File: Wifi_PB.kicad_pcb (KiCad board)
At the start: 2 copper layers, 100 x 49.7 mm, 163 parts, among them P1 CONN_01X02, P10 CONN_01X01, P12 CONN_01X04, P13 CONN_01X04, P14 CONN_01X04, P15 USB_MINI, P16 CONN_01X01, P17 CONN_01X01, P18 CONN_01X01, P19 CONN_01X01, P2 CONN_01X03, P3 CONN_01X03, P4 CONN_01X03, P5 CONN_01X03, P6 CONN_01X01, P7 CONN_01X01, P8 CONN_01X01, P9 CONN_01X01, Q1 SMBT3904, Q10 BC849, Q11 NX2301P, Q2 SMBT3904, Q3 BSS138, Q4 BSS138, Q5 SMBT3904, Q6 SMBT3904, Q7 SMBT3904, Q8 SMBT3904, Q9 SMBT3904, SW1 Pulsador_2p, SW2 Pulsador_2p, SW3 Pulsador_2p, SW4 Pulsador_2p, U1 MCP73831T, U10 Matriz_5x7_Anodo_Filas, U11 40106, U12 MCP1640, U2 LD1117S33TR, U3 CH340G, U4 ESP8266, U5 MMA7660FC, U6 MCP23017, U7 MCP23017, U8 MCP3204, U9 PCA9551, Y1 Cristal

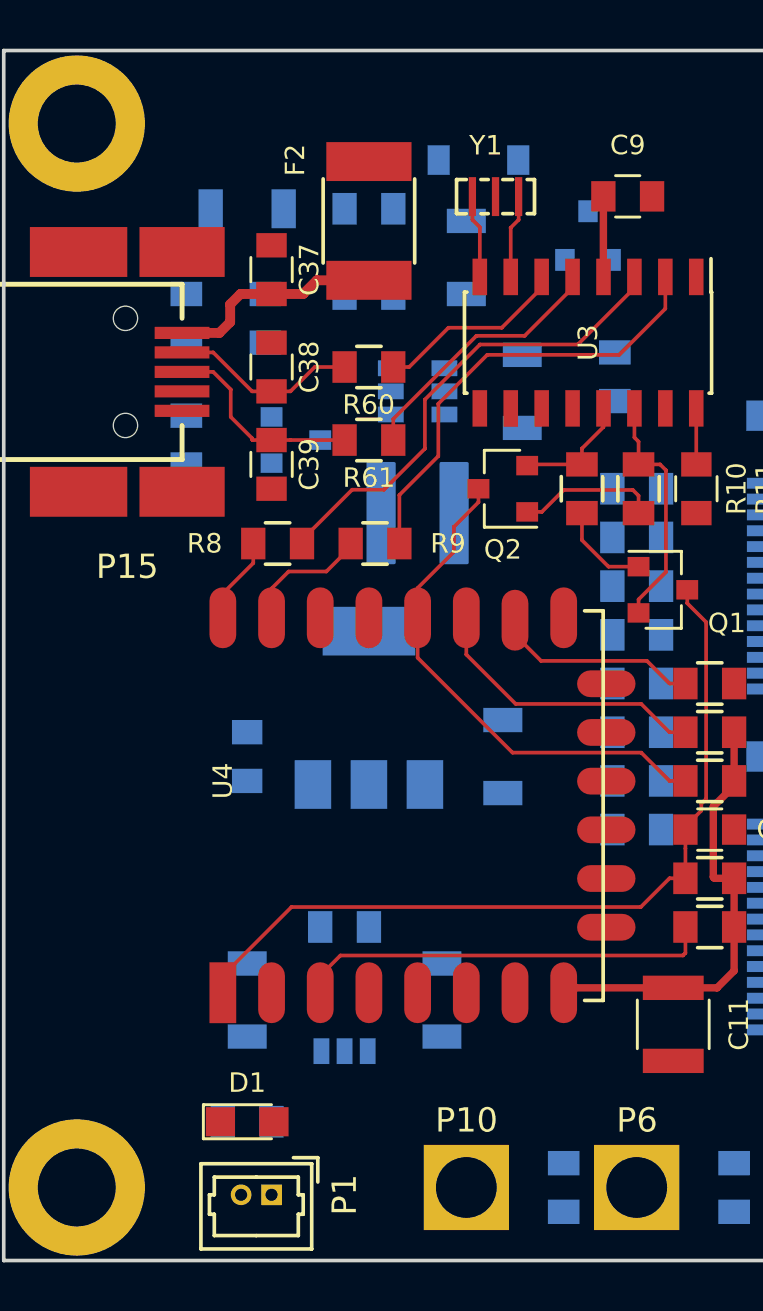
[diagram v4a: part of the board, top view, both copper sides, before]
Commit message: realizado el trazado de los reguladores
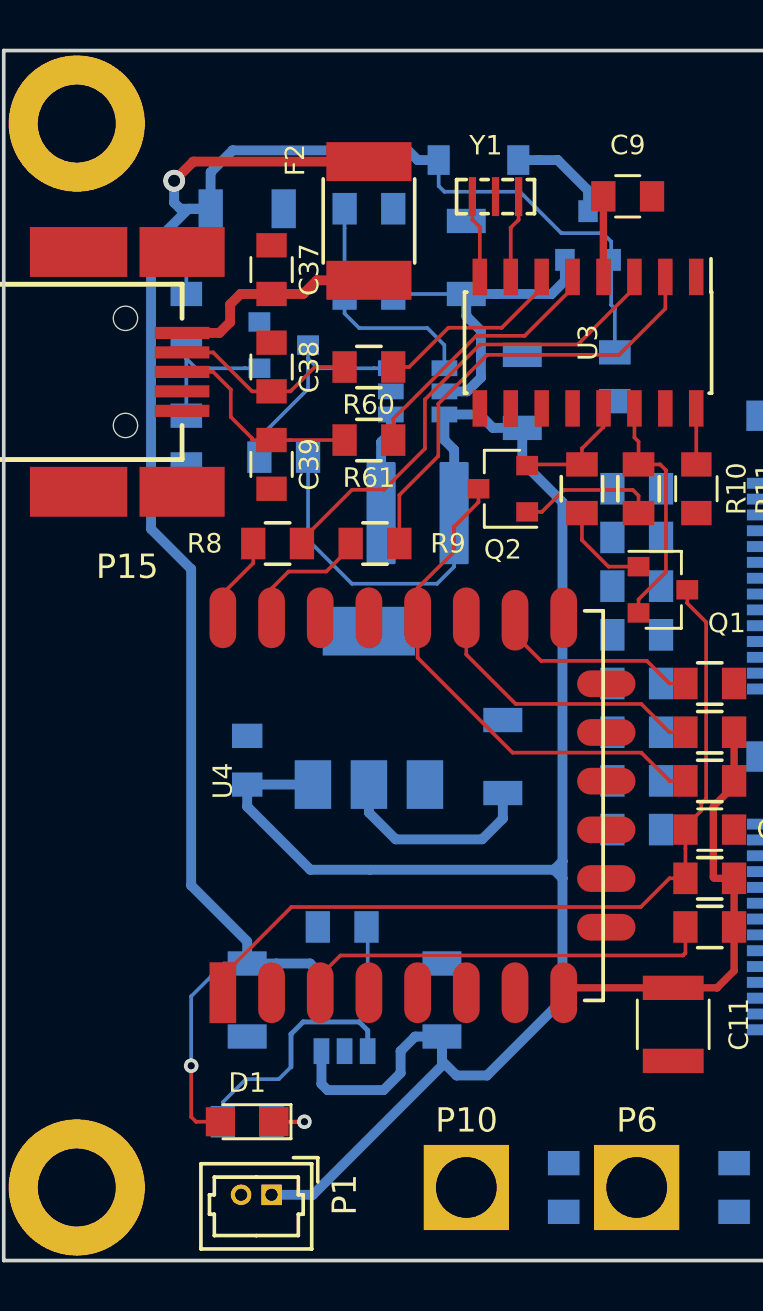
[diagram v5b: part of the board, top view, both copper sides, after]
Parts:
- moved R56 5.75 mm to (65.5, 51.7), turned to 0 degrees
- moved Q10 3.93 mm to (65.5, 47.1)
- moved C2 0.15 mm to (64.0, 64.2)
- moved R2 0.10 mm to (67.9, 71.0)
- turned D1 to 180 degrees
- turned R1 to 0 degrees
- turned R55 to 270 degrees
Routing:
- net VBATT: track 0.00 -> 88.5 mm
- net VUSB: track 0.00 -> 87.3 mm, vias 0 -> 2
- net V5VBOOST: track 0.00 -> 13.5 mm
- net Net-(R1-Pad1): track 0.00 -> 9.90 mm
- net Net-(R57-Pad2): track 0.00 -> 9.89 mm
- net Net-(Q10-Pad3): track 0.00 -> 8.99 mm
- net +3V3: track 21.8 -> 30.3 mm
- net Net-(Q10-Pad1): track 0.00 -> 6.16 mm
- net +5V: track 2.30 -> 6.54 mm
- net Net-(L2-Pad2): track 0.00 -> 4.22 mm
- net Net-(R2-Pad1): track 0.00 -> 2.99 mm
- net Net-(D1-Pad1): track 0.00 -> 2.60 mm, vias 0 -> 1

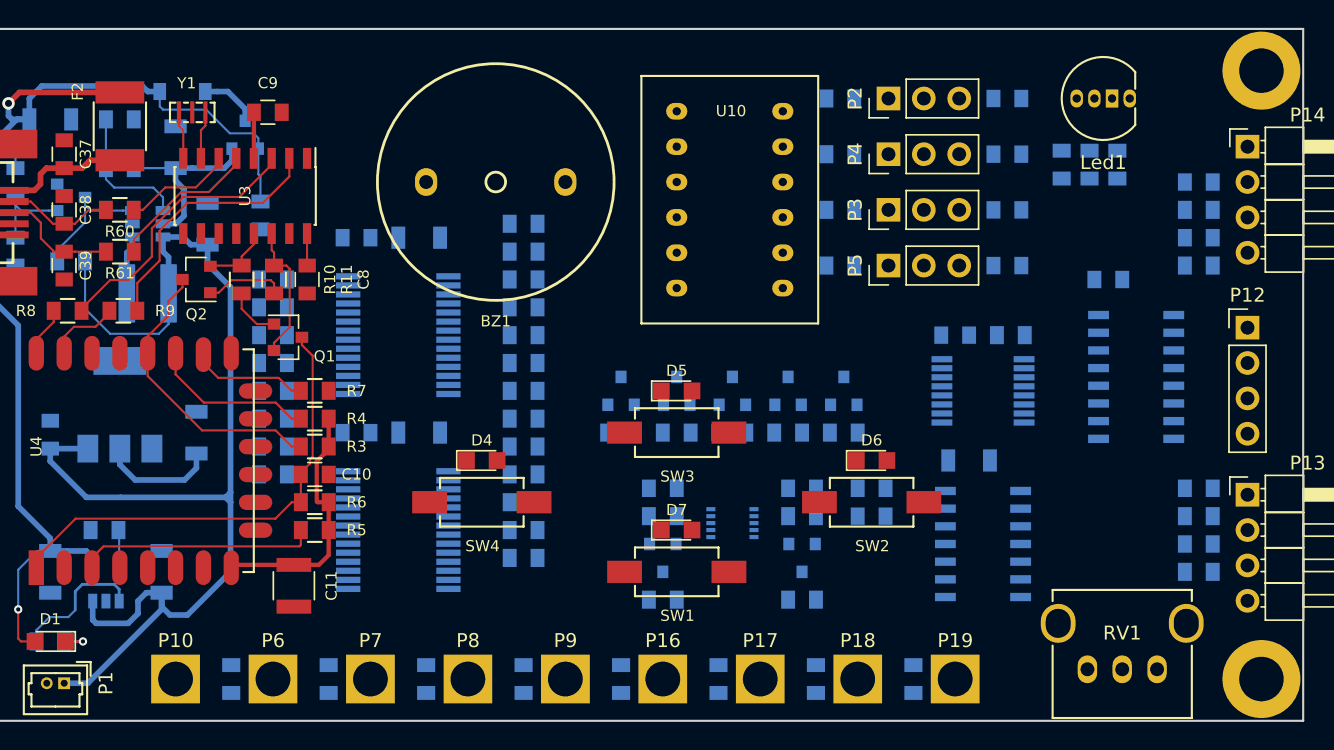
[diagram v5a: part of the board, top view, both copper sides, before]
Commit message: modificado conexion led rgb para mejorar trazado
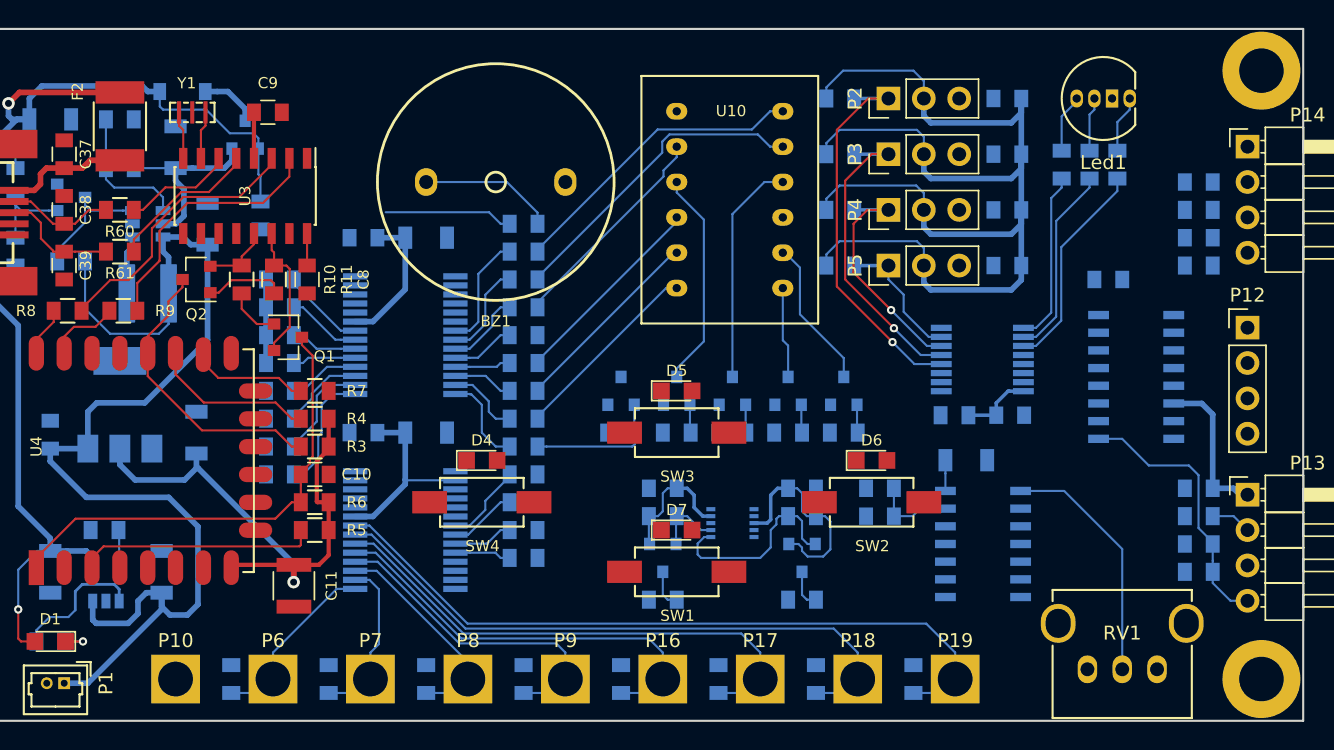
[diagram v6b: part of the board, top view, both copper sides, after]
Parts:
- moved R16 7.03 mm to (129.0, 62.7)
- moved C21 6.98 mm to (133.0, 62.7)
- moved R22 6.02 mm to (80.5, 67.0)
- moved R25 6.02 mm to (80.5, 61.0)
- moved P3 4.00 mm to (124.2, 44.0)
- moved P4 4.00 mm to (124.2, 48.0)
- moved U9 2.25 mm to (131.0, 58.7), turned to 0 degrees
- moved R23 2.06 mm to (80.5, 65.0)
- moved R24 2.06 mm to (80.5, 63.0)
- moved C18 0.60 mm to (123.6, 70.0)
- moved C19 0.60 mm to (123.6, 68.0)
- moved C14 0.50 mm to (91.0, 50.0)
- moved C15 0.50 mm to (91.0, 64.0)
- moved C16 0.50 mm to (86.5, 50.0)
- moved C17 0.50 mm to (86.5, 64.0)
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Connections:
- U9 pad 11: LED_GREEN -> LED_RED
- U9 pad 9: LED_RED -> LED_GREEN
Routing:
- net +5V: track 6.54 -> 152.2 mm
- net PD7: track 0.00 -> 52.2 mm
- net +3V3: track 30.3 -> 75.3 mm, vias 0 -> 1
- net PD6: track 0.00 -> 44.9 mm
- net PD5: track 0.00 -> 37.7 mm
- net PD4: track 0.00 -> 30.4 mm
- net SERVO1: track 0.00 -> 28.2 mm, vias 0 -> 1
- net PD3: track 0.00 -> 23.1 mm
- net Net-(R26-Pad1): track 0.00 -> 22.9 mm
- net SERVO2: track 0.00 -> 22.6 mm, vias 0 -> 1
- net Net-(R31-Pad1): track 0.00 -> 21.9 mm
- net Net-(C31-Pad1): track 0.00 -> 19.5 mm
- net CH0: track 0.00 -> 17.7 mm
- net SERVO3: track 0.00 -> 17.4 mm, vias 0 -> 1
- net Net-(Q7-Pad3): track 0.00 -> 16.3 mm
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
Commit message: añadida LDR. Finalizado trazado provisional
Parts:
- added Gnd-Via: VAL**, Vias:Gnd-Via, F.Cu at (64.1, 69.0)
- added Gnd-Via: VAL**, Vias:Gnd-Via, F.Cu at (110.4, 74.6)
- added Gnd-Via: VAL**, Vias:Gnd-Via, F.Cu at (110.3, 77.6)
- added Gnd-Via: VAL**, Vias:Gnd-Via, F.Cu at (102.3, 75.9)
- added Gnd-Via: VAL**, Vias:Gnd-Via, F.Cu at (100.1, 74.8)
- added Gnd-Via: VAL**, Vias:Gnd-Via, F.Cu at (112.2, 69.5)
- added Gnd-Via: VAL**, Vias:Gnd-Via, F.Cu at (113.6, 71.1)
- added Gnd-Via: VAL**, Vias:Gnd-Via, F.Cu at (121.1, 67.6)
- added Gnd-Via: VAL**, Vias:Gnd-Via, F.Cu at (74.1, 56.4)
- added Gnd-Via: VAL**, Vias:Gnd-Via, F.Cu at (76.3, 62.7)
- added Gnd-Via: VAL**, Vias:Gnd-Via, F.Cu at (77.6, 56.2)
- added Gnd-Via: VAL**, Vias:Gnd-Via, F.Cu at (67.8, 67.5)
- added Gnd-Via: VAL**, Vias:Gnd-Via, F.Cu at (76.4, 55.8)
- added Gnd-Via: VAL**, Vias:Gnd-Via, F.Cu at (86.8, 48.0)
- added Gnd-Via: VAL**, Vias:Gnd-Via, F.Cu at (78.4, 57.9)
- added Gnd-Via: VAL**, Vias:Gnd-Via, F.Cu at (76.7, 76.5)
- added Gnd-Via: VAL**, Vias:Gnd-Via, F.Cu at (92.5, 64.6)
- added Gnd-Via: VAL**, Vias:Gnd-Via, F.Cu at (92.3, 71.0)
- added Gnd-Via: VAL**, Vias:Gnd-Via, F.Cu at (103.5, 69.9)
- added Gnd-Via: VAL**, Vias:Gnd-Via, F.Cu at (92.6, 62.4)
- added Gnd-Via: VAL**, Vias:Gnd-Via, F.Cu at (96.2, 67.9)
- added R47: LDR, Sensores:LDR_TOKEN_PGM5_Series, F.Cu at (141.0, 69.4)
- added R48: 1K, Resistencias:R_0805, B.Cu at (136.7, 72.0)
- moved Q5 1.69 mm to (106.6, 60.5)
- moved Q6 1.69 mm to (110.6, 60.5)
- moved Q7 1.69 mm to (114.6, 60.5)
- moved Q8 1.69 mm to (118.6, 60.5)
- moved Q9 1.69 mm to (122.6, 60.5)
- moved R29 1.69 mm to (106.6, 63.5)
- moved R30 1.69 mm to (110.6, 63.5)
- moved R35 1.69 mm to (114.6, 63.5)
- moved R36 1.69 mm to (118.6, 63.5)
- moved R37 1.69 mm to (122.6, 63.5)
- moved C14 1.30 mm to (92.3, 50.0)
- moved C15 1.30 mm to (92.3, 64.0)
- moved C16 1.30 mm to (87.8, 50.0)
- moved C17 1.30 mm to (87.8, 64.0)
- moved R21 1.30 mm to (99.3, 65.0)
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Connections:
- P15 pad 6: Net-(P15-Pad6) -> GND
- U11 pad 10: (no net) -> PC7
- U11 pad 11: (no net) -> Net-(C33-Pad1)
- U11 pad 3: Net-(C33-Pad1) -> (no net)
- U11 pad 4: PC7 -> (no net)
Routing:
- net +5V: track 152.2 -> 481.5 mm, vias 0 -> 15
- net +3V3: track 75.3 -> 172.0 mm, vias 1 -> 4
- net SCL: track 14.3 -> 104.9 mm, vias 0 -> 3
- net SDA: track 4.88 -> 88.6 mm, vias 0 -> 3
- net SCK: track 0.00 -> 70.1 mm, vias 0 -> 1
- net MISO: track 0.00 -> 65.3 mm, vias 0 -> 1
- net PC7: track 0.00 -> 64.9 mm, vias 0 -> 2
- net SCL2: track 2.80 -> 65.3 mm, vias 0 -> 4
- net PC4: track 0.00 -> 61.5 mm, vias 0 -> 1
- net PC5: track 0.00 -> 61.2 mm, vias 0 -> 1
- net MOSI: track 0.00 -> 58.7 mm, vias 0 -> 1
- net PC6: track 0.00 -> 55.1 mm, vias 0 -> 2
- net BUZZER: track 9.71 -> 64.6 mm, vias 0 -> 1
- net SDA2: track 2.80 -> 55.9 mm, vias 0 -> 4
- net Net-(Q9-Pad1): track 2.02 -> 51.7 mm, vias 0 -> 2
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
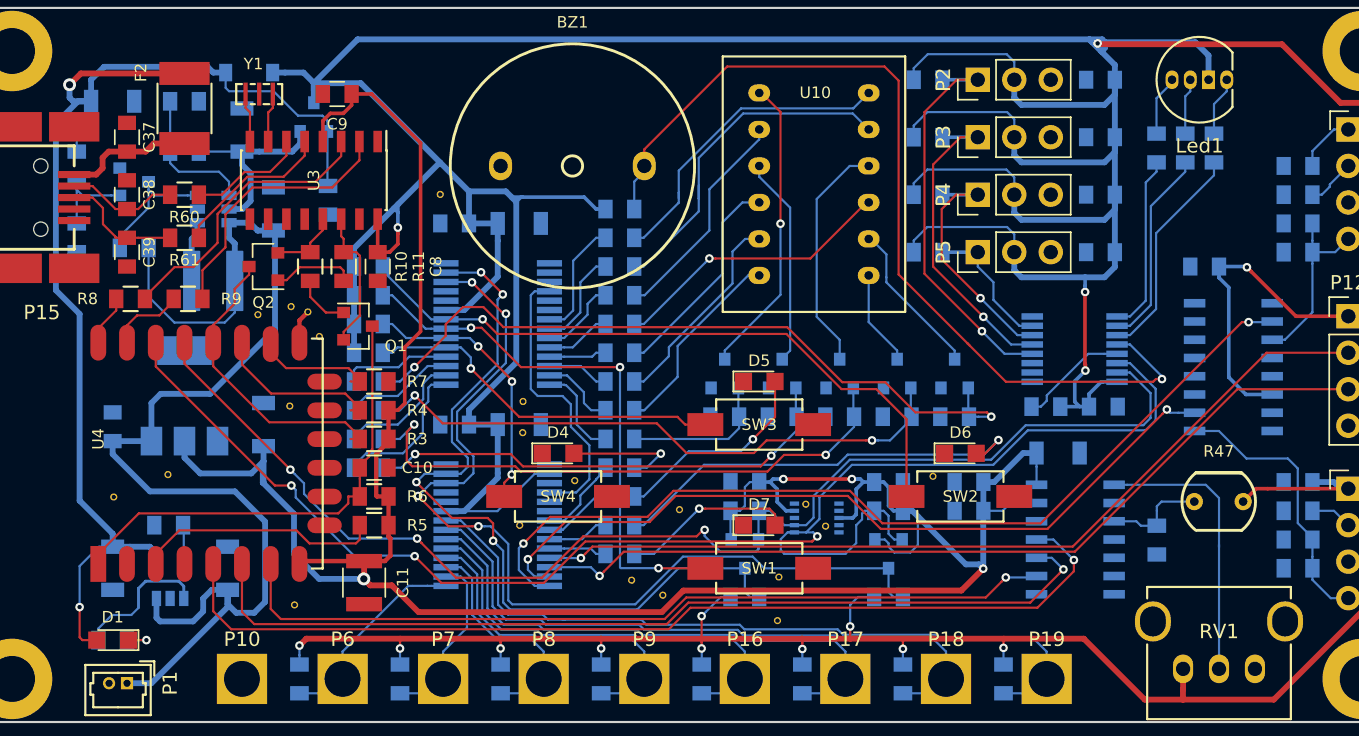
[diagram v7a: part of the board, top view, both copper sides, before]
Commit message: añadidos logos a la serigrafia
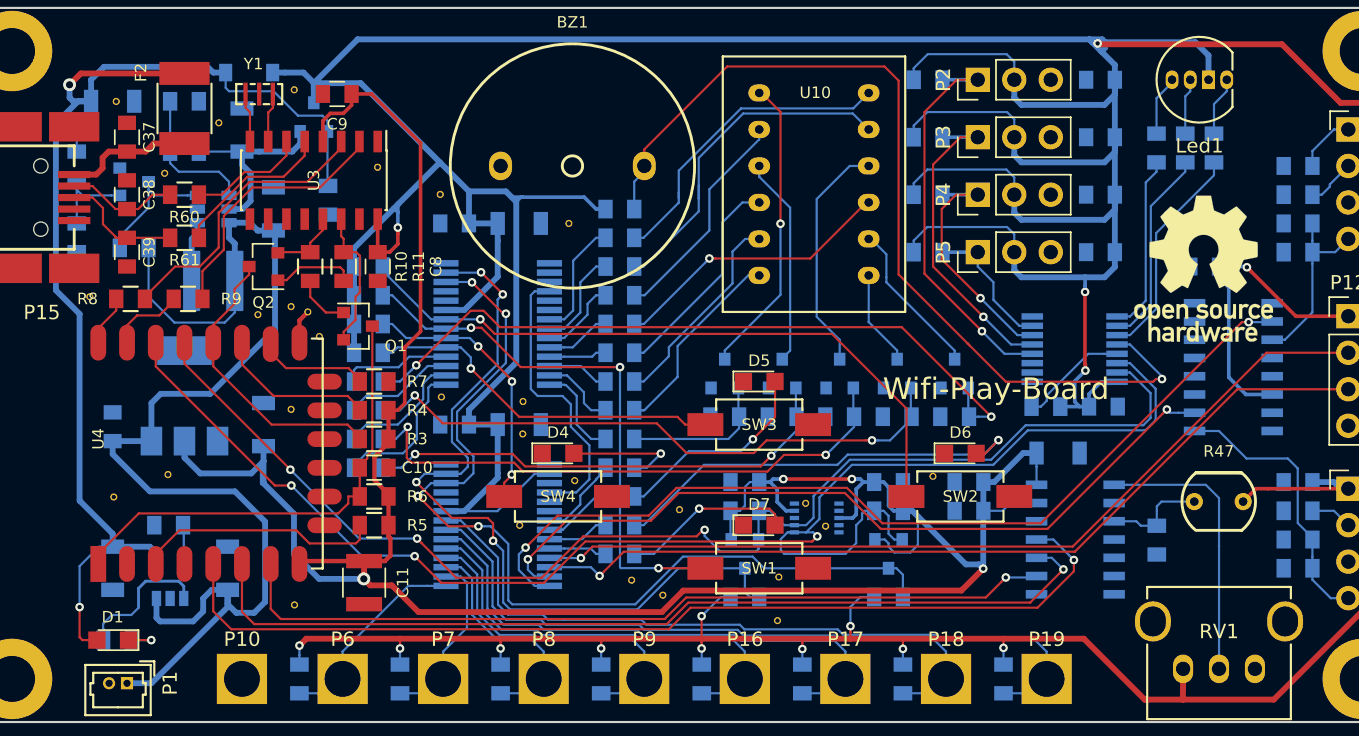
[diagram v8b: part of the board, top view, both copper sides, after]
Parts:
- added G***: KiCad Logo, logos:KiCad-Logo_11mmx5mm, B.Cu at (57.0, 65.9)
- added G***: LOGO, logos:logo_HackLabAl, B.Cu at (95.4, 40.7)
- added G***: LOGO, logos:osh-logo, F.Cu at (139.9, 53.1)
- added Gnd-Via: VAL**, Vias:Gnd-Via, F.Cu at (86.9, 62.1)
- added Gnd-Via: VAL**, Vias:Gnd-Via, F.Cu at (95.8, 50.0)
- added Gnd-Via: VAL**, Vias:Gnd-Via, F.Cu at (62.4, 55.1)
- added Gnd-Via: VAL**, Vias:Gnd-Via, F.Cu at (76.6, 40.7)
- added Gnd-Via: VAL**, Vias:Gnd-Via, F.Cu at (82.4, 46.1)
- added Gnd-Via: VAL**, Vias:Gnd-Via, F.Cu at (71.4, 43.0)
- added Gnd-Via: VAL**, Vias:Gnd-Via, F.Cu at (64.2, 41.5)
- added Gnd-Via: VAL**, Vias:Gnd-Via, F.Cu at (67.6, 46.5)
- moved R1 0.34 mm to (64.3, 79.0)
- moved Gnd-Via 0.25 mm to (76.4, 62.9)
- moved Gnd-Via 0.09 mm to (92.5, 64.7)
- moved Gnd-Via 0.06 mm to (112.2, 69.5)
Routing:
- net Net-(Q7-Pad1): track 41.0 -> 40.0 mm
- net /Control/GPIO2: track 11.1 -> 10.4 mm
- net Net-(Q9-Pad1): track 51.7 -> 51.0 mm
- net /Control/GPIO15: track 7.83 -> 7.18 mm
- net /Control/GPIO0: track 21.1 -> 20.4 mm
- net Net-(R9-Pad2): track 18.7 -> 18.2 mm
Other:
- board text added: "Wifi-Play-Board"
